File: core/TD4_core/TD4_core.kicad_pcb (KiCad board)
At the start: 2 copper layers, 94 parts, among them J1 Conn_02x32_Row_Letter_First, J2 Conn_01x04, J3 Conn_01x04, J4 Conn_01x04, U1 74HC161, U10 74LS151, U11 74AHC1G04, U12 74AHC1G04, U13 74AHC1G86, U14 74AHC1G04, U15 74AHC1G86, U16 74HC86, U17 74HC04, U18 74HC21, U19 74HC86, U2 74HC161, U20 74HC04, U21 74HC86, U22 74HC04, U23 74HC86, U24 74HC04, U25 74HC21, U26 74HC86, U27 74HC04, U28 74HC21, U29 74HC153, U3 74HC161, U30 74HC153, U31 74HC74, U32 74HC175, U33 74AHC1G08, U34 74HC125, U35 74HC175, U36 74AHC1G08, U37 74HC155, U38 74HC125, U39 74HC125, U4 74HC161, U40 74HC125, U5 74HC86, U6 74HC08, U7 74HC32, U8 74HC86, U9 74HC08

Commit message: Adder and decoder done
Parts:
- moved C16 294.7 mm to (147.7, 138.2), turned to 90 degrees
- moved U14 294.2 mm to (143.5, 143.5)
- moved U12 294.2 mm to (143.5, 137.2)
- moved C20 293.5 mm to (146.4, 144.5), turned to 270 degrees
- moved U13 291.6 mm to (143.5, 156.2)
- moved C17 290.9 mm to (146.4, 157.2), turned to 270 degrees
- moved U15 259.9 mm to (110.4, 169.9)
- moved C21 259.4 mm to (113.3, 170.9), turned to 270 degrees
- moved U10 248.8 mm to (91.4, 154.9)
- moved C18 235.3 mm to (91.4, 146.1), turned to 180 degrees
- moved U11 233.1 mm to (80.6, 157.6)
- moved C19 228.5 mm to (83.7, 158.5), turned to 270 degrees
- moved U33 149.4 mm to (-38.2, 197.2), turned to 180 degrees
- moved C39 145.5 mm to (-41.4, 196.2), turned to 90 degrees
- moved U32 140.8 mm to (-49.0, 192.2)
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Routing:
- net /Ins2: track 19.2 -> 204.3 mm, vias 3 -> 18
- net /Ins3: track 18.5 -> 171.6 mm, vias 3 -> 16
- net GND: track 573.6 -> 724.2 mm, vias 20 -> 24
- net VCC: track 426.3 -> 560.0 mm, vias 14 -> 21
- net /Ins0: track 9.26 -> 129.7 mm, vias 1 -> 7
- net /Ins1: track 9.71 -> 117.2 mm, vias 1 -> 5
- net /Instruction decoder/3state_e: track 24.6 -> 74.3 mm, vias 3 -> 5
- net /Instruction decoder/sheet5C66DD7A/B2: track 0.00 -> 36.4 mm, vias 0 -> 2
- net /Instruction decoder/Sheet5C668719/B2: track 0.00 -> 36.4 mm, vias 0 -> 2
- net /Instruction decoder/sheet5C66DD7A/B3: track 0.00 -> 30.9 mm, vias 0 -> 2
- net /Instruction decoder/Sheet5C668719/B3: track 0.00 -> 30.6 mm, vias 0 -> 2
- net /Instruction decoder/sheet5C66DD7A/B1: track 0.00 -> 30.3 mm, vias 0 -> 2
- net /Instruction decoder/Sheet5C668719/B1: track 0.00 -> 29.9 mm, vias 0 -> 2
- net /Instruction decoder/sheet5C67666E/Q0: track 0.00 -> 25.4 mm, vias 0 -> 2
- net /Instruction decoder/sheet5C66DD7A/B0: track 0.00 -> 23.7 mm, vias 0 -> 2
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
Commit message: Minor core blocks routed
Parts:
- moved U40 454.2 mm to (309.7, 36.7)
- moved C46 454.2 mm to (315.2, 33.0)
- moved J4 417.6 mm to (334.9, 34.2)
- moved J2 345.8 mm to (132.2, -15.9)
- moved J3 292.1 mm to (134.0, 17.7)
- moved C44 262.9 mm to (120.0, -17.0)
- moved U38 262.9 mm to (114.6, -13.3)
- moved U37 192.2 mm to (58.4, 108.0)
- moved C43 187.0 mm to (58.3, 100.3)
- moved C45 177.1 mm to (119.7, 16.5)
- moved U39 177.1 mm to (114.3, 20.2)
- moved C8 157.1 mm to (72.4, 27.9), turned to 180 degrees
- moved C7 154.2 mm to (72.4, 11.4), turned to 180 degrees
- moved C10 154.0 mm to (72.4, 61.0), turned to 180 degrees
- moved U3 151.9 mm to (72.4, 53.3)
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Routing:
- net GND: track 724.2 -> 834.7 mm, vias 24 -> 30
- net VCC: track 560.0 -> 657.2 mm, vias 21 -> 25
- net /Ins2: track 204.3 -> 203.4 mm

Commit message: Routed most of data path
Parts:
- J1: moved to B.Cu
- moved C6 216.4 mm to (33.3, 132.3), turned to 270 degrees
- moved C4 216.3 mm to (34.5, 56.1), turned to 90 degrees
- moved C5 214.7 mm to (34.5, 101.9), turned to 90 degrees
- moved C3 212.8 mm to (36.8, 132.3), turned to 270 degrees
- moved C2 209.9 mm to (38.4, 101.9), turned to 90 degrees
- moved C1 199.9 mm to (38.4, 56.1), turned to 90 degrees
- moved U38 164.0 mm to (254.0, 73.2)
- moved J1 161.3 mm to (27.9, 54.9), turned to 270 degrees
- moved J2 158.1 mm to (265.4, 69.3)
- moved C44 156.7 mm to (254.0, 64.3), turned to 180 degrees
- moved U39 156.0 mm to (254.0, 89.7)
- moved C45 148.9 mm to (254.0, 80.8), turned to 180 degrees
- moved J3 148.1 mm to (265.4, 85.9)
- moved R1 139.6 mm to (-19.5, 82.6)
- moved R2 139.6 mm to (-16.1, 82.6)
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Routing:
- net /Multiplexer 4x 4->1/B1: track 0.00 -> 216.0 mm, vias 0 -> 10
- net /Multiplexer 4x 4->1/B3: track 0.00 -> 215.8 mm, vias 0 -> 10
- net GND: track 834.7 -> 1048.1 mm, vias 30 -> 38
- net /Multiplexer 4x 4->1/B2: track 0.00 -> 205.2 mm, vias 0 -> 8
- net /Multiplexer 4x 4->1/A3: track 0.00 -> 201.4 mm, vias 0 -> 12
- net /Multiplexer 4x 4->1/B0: track 0.00 -> 198.4 mm, vias 0 -> 10
- net VCC: track 657.2 -> 849.7 mm, vias 25 -> 36
- net /Multiplexer 4x 4->1/A2: track 0.00 -> 191.6 mm, vias 0 -> 10
- net /Multiplexer 4x 4->1/A1: track 0.00 -> 175.6 mm, vias 0 -> 8
- net /Multiplexer 4x 4->1/A0: track 0.00 -> 160.4 mm, vias 0 -> 8
- net /~DEBUG_ON~: track 0.00 -> 139.4 mm, vias 0 -> 12
- net /RAM_D0: track 0.00 -> 89.3 mm, vias 0 -> 5
- net /Register selector/Q0: track 0.00 -> 86.8 mm, vias 0 -> 4
- net /RAM_D1: track 0.00 -> 81.6 mm, vias 0 -> 5
- net /RAM_D3: track 0.00 -> 81.2 mm, vias 0 -> 5
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
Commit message: Started tieing it all together
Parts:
- moved U35 159.2 mm to (61.0, 161.3)
- moved C42 159.2 mm to (61.0, 152.4)
- moved C41 159.2 mm to (65.9, 165.7)
- moved U36 159.2 mm to (70.1, 166.8)
- moved C38 120.3 mm to (61.0, 135.9)
- moved C39 120.3 mm to (68.6, 147.6)
- moved U32 120.3 mm to (61.0, 143.5)
- moved U33 120.3 mm to (71.8, 148.6)
- moved R1 75.1 mm to (52.1, 59.9)
- moved R2 75.1 mm to (55.5, 59.9)
- moved R3 75.1 mm to (58.9, 59.9)
- moved R4 75.1 mm to (62.3, 59.9)
- moved C16 72.8 mm to (175.6, 107.7)
- moved C22 72.8 mm to (138.4, 62.2)
- moved C23 72.8 mm to (148.6, 62.2)
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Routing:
- net /IN1: track 0.00 -> 59.1 mm, vias 0 -> 1
- net /IN0: track 0.00 -> 51.1 mm, vias 0 -> 1
- net /IN3: track 0.00 -> 49.7 mm, vias 0 -> 1
- net /IN2: track 0.00 -> 44.5 mm, vias 0 -> 1
- net VCC: track 849.7 -> 873.2 mm, vias 36 -> 39
- net GND: track 1048.1 -> 1054.8 mm

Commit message: Core routed
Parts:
- moved R1 72.3 mm to (123.4, 47.9), turned to 270 degrees
- moved R2 72.2 mm to (126.7, 47.9), turned to 270 degrees
- moved R3 72.1 mm to (130.0, 47.9), turned to 270 degrees
- moved R4 72.0 mm to (133.3, 47.9), turned to 270 degrees
- moved C39 50.5 mm to (94.7, 104.4)
- moved U33 50.5 mm to (97.9, 105.4)
- moved C38 50.5 mm to (87.1, 92.7)
- moved U32 50.5 mm to (87.1, 100.3)
- moved C41 44.5 mm to (90.8, 128.9)
- moved C42 44.5 mm to (85.9, 115.6)
- moved U36 44.5 mm to (95.0, 129.9)
- moved U35 44.5 mm to (85.9, 124.5)
- moved C3 36.9 mm to (73.7, 129.5)
- moved C6 36.9 mm to (70.1, 129.5)
- moved C1 35.7 mm to (73.9, 53.3)
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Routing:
- net ~RESET: track 0.00 -> 419.4 mm, vias 0 -> 9
- net CLK: track 0.00 -> 366.6 mm, vias 0 -> 7
- net GND: track 1054.8 -> 1340.2 mm, vias 38 -> 48
- net /RAM_A3: track 62.0 -> 344.0 mm, vias 3 -> 10
- net /RAM_A2: track 50.9 -> 330.6 mm, vias 2 -> 12
- net VCC: track 873.2 -> 1147.2 mm, vias 39 -> 46
- net /RAM_A1: track 34.7 -> 298.5 mm, vias 3 -> 10
- net /RAM_A0: track 25.4 -> 286.1 mm, vias 2 -> 8
- net /RAM_D0: track 89.3 -> 319.7 mm, vias 5 -> 7
- net /RAM_D1: track 81.6 -> 306.8 mm, vias 5 -> 7
- net /RAM_D2: track 79.9 -> 296.8 mm, vias 5 -> 7
- net /RAM_D3: track 81.2 -> 293.6 mm, vias 5 -> 7
- net /~DEBUG_ON~: track 139.4 -> 320.3 mm
- net /RAM_RW: track 0.00 -> 166.9 mm, vias 0 -> 3
- net /RAM_WE: track 0.00 -> 157.8 mm, vias 0 -> 3
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
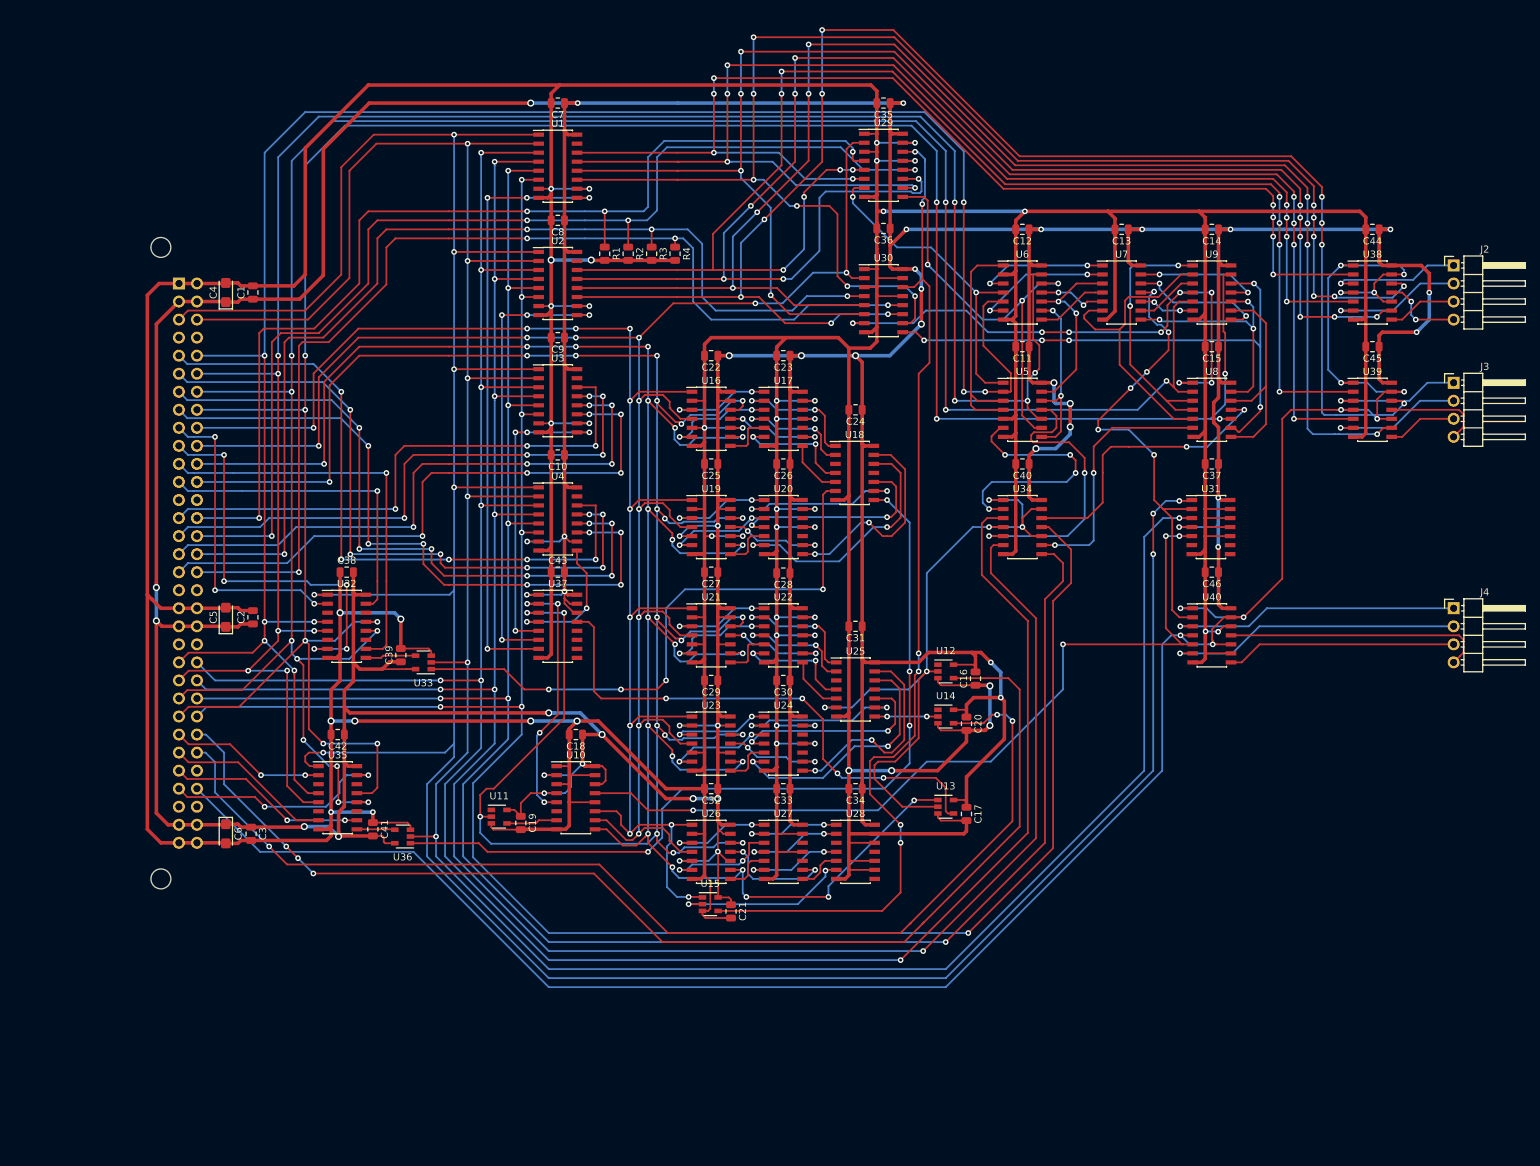
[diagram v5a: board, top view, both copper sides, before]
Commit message: DRC violations fixed; edge cuts added
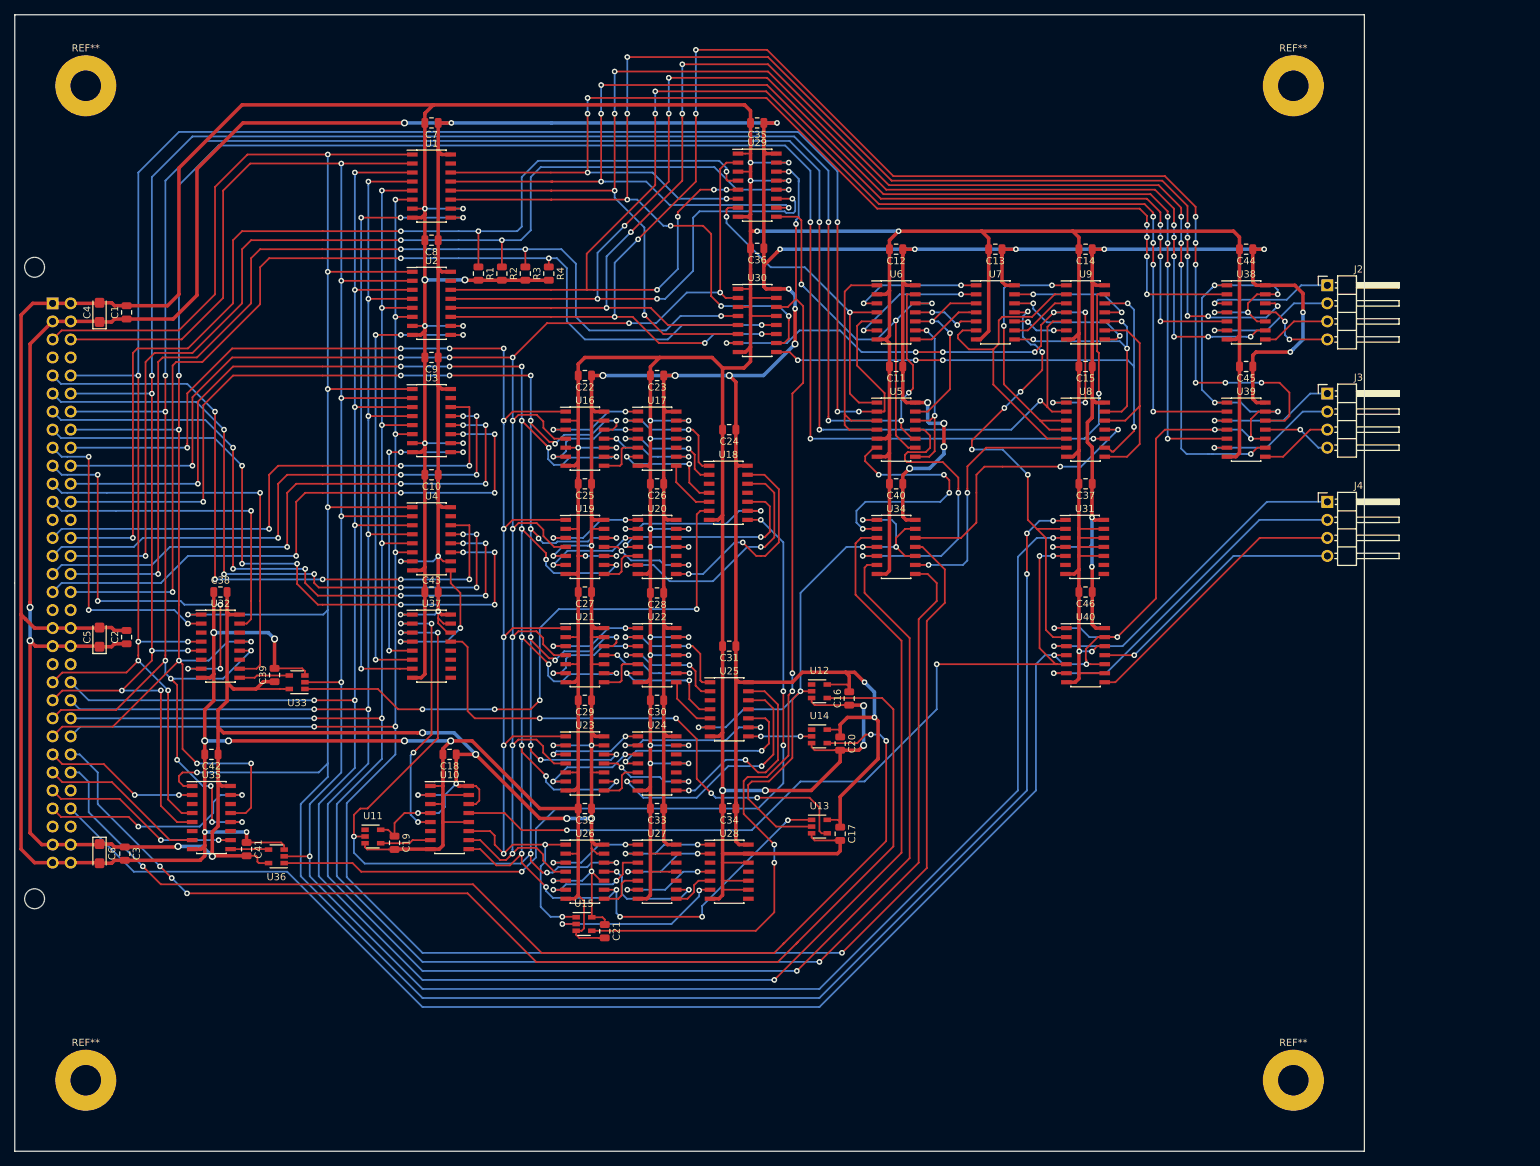
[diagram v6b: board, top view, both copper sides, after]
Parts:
- added REF**: MountingHole_4.3mm_M4_Pad, MountingHole:MountingHole_4.3mm_M4_Pad, F.Cu at (220.4, 24.2)
- added REF**: MountingHole_4.3mm_M4_Pad, MountingHole:MountingHole_4.3mm_M4_Pad, F.Cu at (220.4, 164.2)
- added REF**: MountingHole_4.3mm_M4_Pad, MountingHole:MountingHole_4.3mm_M4_Pad, F.Cu at (50.4, 164.2)
- added REF**: MountingHole_4.3mm_M4_Pad, MountingHole:MountingHole_4.3mm_M4_Pad, F.Cu at (50.4, 24.2)
- moved J4 23.3 mm to (225.2, 82.8)
- moved C18 18.0 mm to (101.6, 118.4)
- moved C19 18.0 mm to (93.9, 130.8)
- moved C24 18.0 mm to (141.0, 72.6)
- moved C27 18.0 mm to (120.7, 95.5)
- moved C38 18.0 mm to (69.3, 95.5)
- moved C41 18.0 mm to (73.0, 131.7)
- moved C42 18.0 mm to (68.1, 118.4)
- moved C43 18.0 mm to (99.1, 95.5)
- moved C46 18.0 mm to (191.1, 95.5)
- moved C6 18.0 mm to (52.3, 132.3)
- moved U10 18.0 mm to (101.6, 127.3)
- moved U15 18.0 mm to (120.5, 142.2)
- moved U18 18.0 mm to (140.8, 81.5)
- moved U21 18.0 mm to (120.7, 104.4)
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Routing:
- net /Sheet5C77FFEF/sheet5C78000E/Out1: track 41.8 -> 49.2 mm
- net /Sheet5C77FFEF/sheet5C78000E/Out2: track 32.4 -> 39.8 mm
- net /Sheet5C77FFEF/sheet5C78000E/Out0: track 41.3 -> 48.6 mm
- net /sheet5C74C5BC/Out3: track 14.1 -> 9.78 mm, vias 0 -> 1
- net /sheet5C74C5BC/Out1: track 19.2 -> 19.8 mm
- net /Multiplexer 4x 4->1/B3: track 215.8 -> 215.2 mm, vias 10 -> 12
- net /sheet5C74C5BC/Out2: track 9.78 -> 10.3 mm
- net /sheet5C74C5BC/Out0: track 18.7 -> 19.2 mm
- net /Sheet5C77FFEF/sheet5C78000E/Out3: track 36.7 -> 37.1 mm, vias 0 -> 1
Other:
- board outline added: 190 x 160 mm
